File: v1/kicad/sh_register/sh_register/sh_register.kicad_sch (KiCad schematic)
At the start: 4 parts, among them J1 LNCPU_Type_A_connector,_male,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, U1 74LS194, U2 74LS194, U3 74LS245

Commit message: partial
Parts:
- removed J1: LNCPU_Type_A_connector,_male,_active_low_reset, LNCPU:LNCPU_TYPE_A_MALE, symbol lncpu:LNCPU_Type_A_connector,_male,_active_low_reset
- added J1: OP_{out}, Connector_PinSocket_2.54mm:PinSocket_1x08_P2.54mm_Vertical, symbol lncpu:LNCPU_DBUS_Socket
- added U4: LNCPU Type B Connector, lncpu:LNCPU_Type_B_Header, symbol lncpu:LNCPU_Type_B_Connector
- U1, U2: footprint (none) -> Package_DIP:DIP-16_W7.62mm_LongPads
- U3: value 74LS245 -> 74LS244; footprint (none) -> Package_DIP:DIP-20_W7.62mm_LongPads
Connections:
- net ASYNC_{out}0: now also J1.1 (D0)
- net ASYNC_{out}1: now also J1.2 (D1)
- net ASYNC_{out}2: now also J1.3 (D2)
- net ASYNC_{out}3: now also J1.4 (D3)
- net ASYNC_{out}4: now also J1.5 (D4)
- net ASYNC_{out}5: now also J1.6 (D5)
- net ASYNC_{out}6: now also J1.7 (D6)
- net ASYNC_{out}7: now also J1.8 (D7)
- net DBUS0: now also U4.4 (DBUS_{0})
- net DBUS1: now also U4.6 (DBUS_{1})
- net DBUS2: now also U4.8 (DBUS_{2})
- net DBUS3: now also U4.10 (DBUS_{3})
- net DBUS4: now also U4.12 (DBUS_{4})
- net DBUS5: now also U4.14 (DBUS_{5})
- net DBUS6: now also U4.16 (DBUS_{6})
- net DBUS7: now also U4.18 (DBUS_{7})
- net at U1.16 (VCC), U2.16 (VCC), U3.20 (VCC): now also U4.2 (VCC), U4.24 (VCC); no longer U1.1 (Mr), U1.2 (Dsr), U2.1 (Mr)
- net at U1.10 (S1), U2.10 (S1): now also U4.9 (CTRL_{3})
- net at U1.11 (Cp), U2.11 (Cp): now also U4.21 (CLK1)
- net at U1.8 (GND), U2.7 (Dsl), U2.8 (GND)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: now also U1.2 (Dsr), U4.1 (GND), U4.17 (GND), U4.20 (GND), U4.22 (GND)
- net at U1.9 (S0), U2.9 (S0): now also U4.7 (CTRL_{2})
- net at U3.1 (OEa): now also U4.3 (CTRL_{0})
- net at U3.19 (OEb): now also U4.5 (CTRL_{1})
- new net: U1.1 (Mr), U2.1 (Mr), U4.19 (RST)
- no-connect marks 3 -> 4

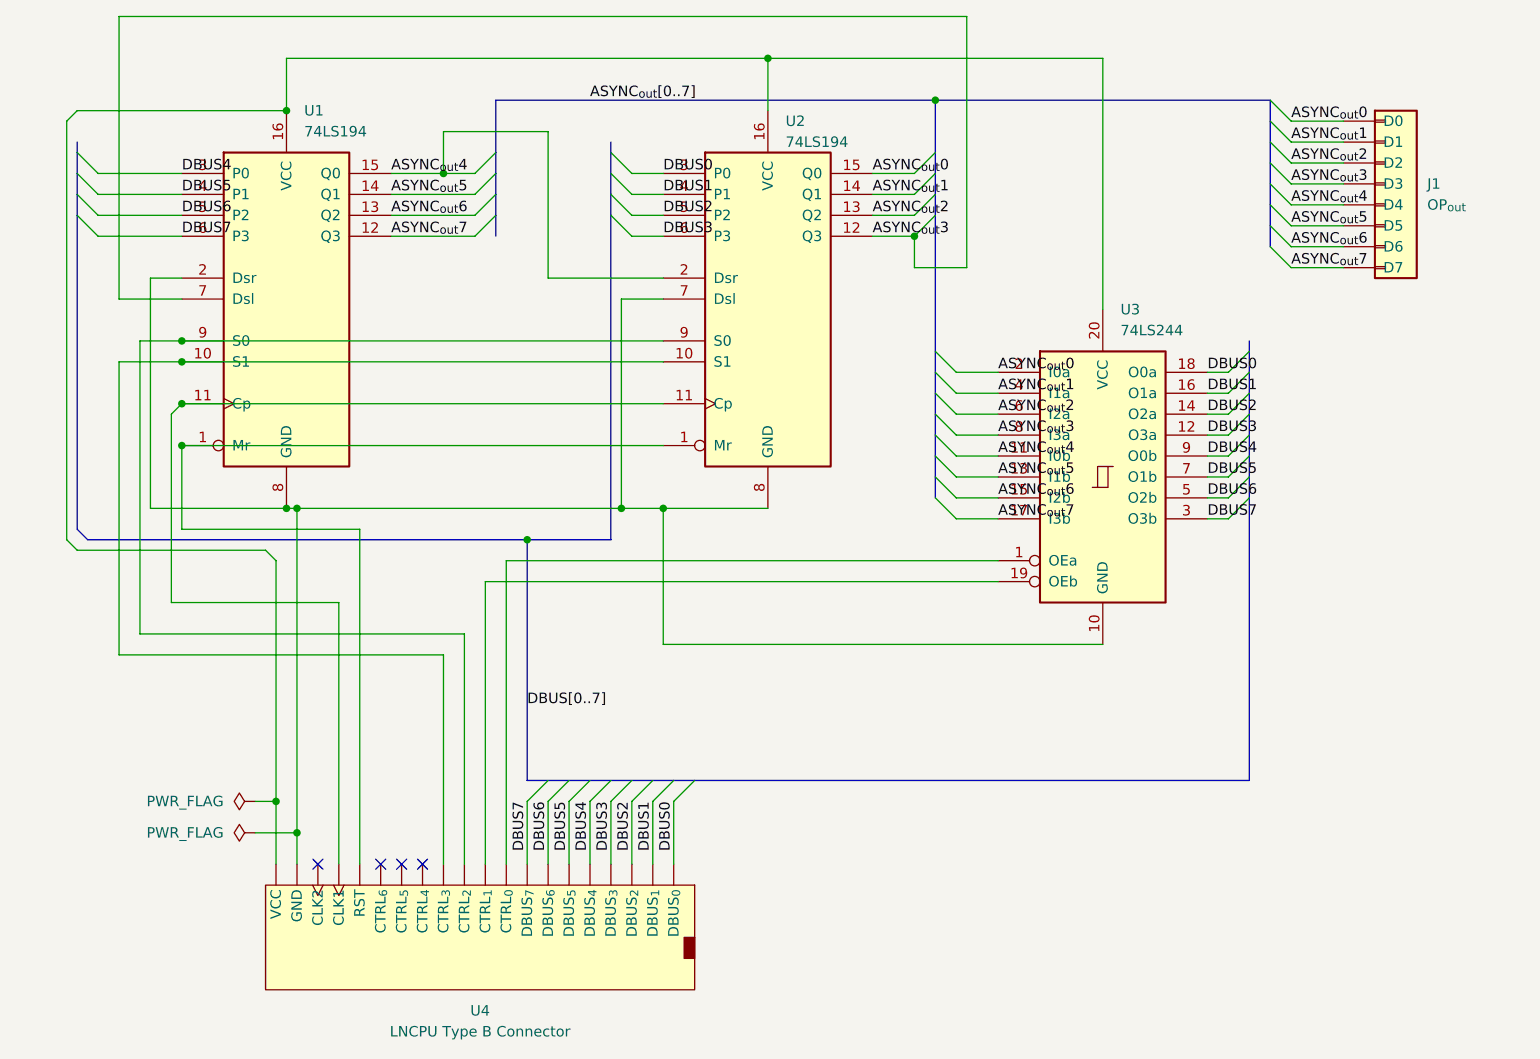
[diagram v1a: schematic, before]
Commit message: check designs for ALU (partial), SP, Shift register, register
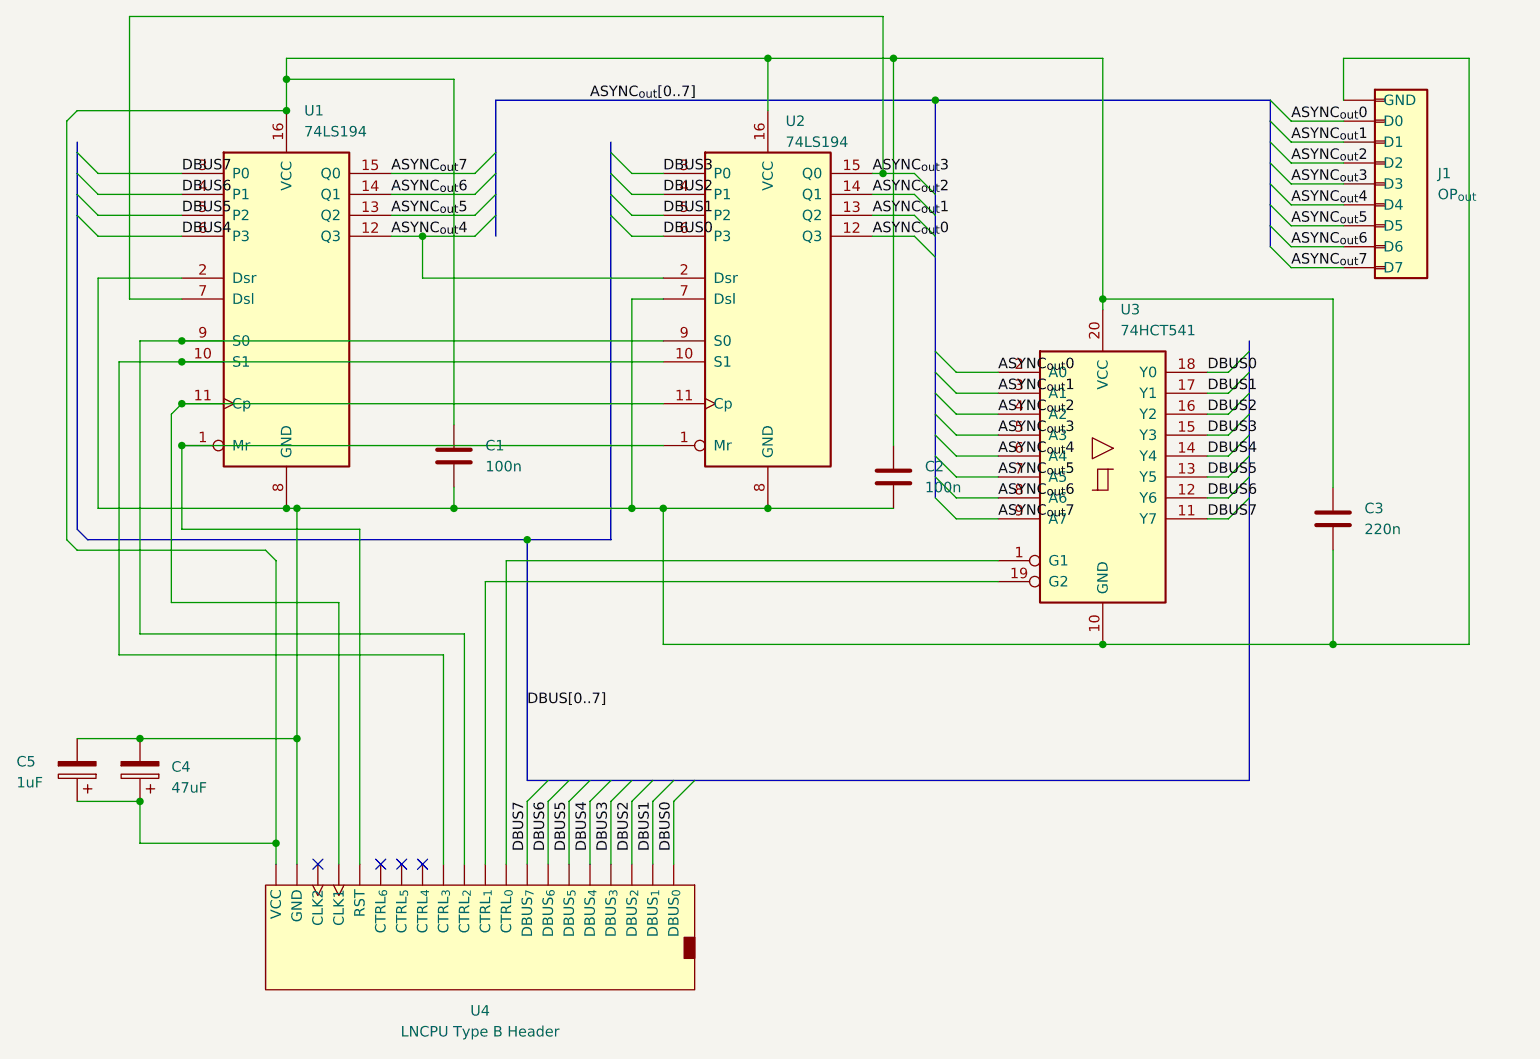
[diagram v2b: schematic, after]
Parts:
- added C1, C2: 100n, Capacitor_THT:C_Disc_D4.3mm_W1.9mm_P5.00mm, symbol Device:C
- added C3: 220n, Capacitor_THT:C_Disc_D4.3mm_W1.9mm_P5.00mm, symbol Device:C
- added C4: 47uF, Capacitor_THT:CP_Radial_D5.0mm_P2.00mm, symbol Device:C_Polarized
- added C5: 1uF, lncpu:CP_Radial_D4.0mm_P2.00mm-Large-Holes, symbol Device:C_Polarized
- J1: footprint Connector_PinSocket_2.54mm:PinSocket_1x08_P2.54mm_Vertical -> Connector_PinSocket_2.54mm:PinSocket_1x10_P2.54mm_Vertical; symbol lncpu:LNCPU_DBUS_Socket -> lncpu:LNCPU_8B_Socket
- U3: value 74LS244 -> 74HCT541; symbol 74xx:74LS244 -> 74xx:74HCT541
- U4: value LNCPU Type B Connector -> LNCPU Type B Header; symbol lncpu:LNCPU_Type_B_Connector -> lncpu:LNCPU_Type_B_Header
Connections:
- net ASYNC_{out}0: now also J1.2 (D0), U2.12 (Q3); no longer J1.1 (D0), U2.15 (Q0)
- net ASYNC_{out}1: now also J1.3 (D1), U2.13 (Q2), U3.3 (A1); no longer J1.2 (D1), U2.14 (Q1), U3.4 (I1a)
- net ASYNC_{out}2: now also J1.4 (D2), U2.14 (Q1), U3.4 (A2); no longer J1.3 (D2), U2.13 (Q2), U3.6 (I2a)
- net ASYNC_{out}3: now also J1.5 (D3), U2.15 (Q0), U3.5 (A3); no longer J1.4 (D3), U2.12 (Q3), U3.8 (I3a)
- net ASYNC_{out}4: now also J1.6 (D4), U1.12 (Q3), U3.6 (A4); no longer J1.5 (D4), U1.15 (Q0), U3.11 (I0b)
- net ASYNC_{out}5: now also J1.7 (D5), U1.13 (Q2), U3.7 (A5); no longer J1.6 (D5), U1.14 (Q1), U3.13 (I1b)
- net ASYNC_{out}6: now also J1.8 (D6), U1.14 (Q1), U3.8 (A6); no longer J1.7 (D6), U1.13 (Q2), U3.15 (I2b)
- net ASYNC_{out}7: now also J1.9 (D7), U1.15 (Q0), U3.9 (A7); no longer J1.8 (D7), U1.12 (Q3), U3.17 (I3b)
- net DBUS0: now also U2.6 (P3); no longer U2.3 (P0)
- net DBUS1: now also U2.5 (P2), U3.17 (Y1); no longer U2.4 (P1), U3.16 (O1a)
- net DBUS2: now also U2.4 (P1), U3.16 (Y2); no longer U2.5 (P2), U3.14 (O2a)
- net DBUS3: now also U2.3 (P0), U3.15 (Y3); no longer U2.6 (P3), U3.12 (O3a)
- net DBUS4: now also U1.6 (P3), U3.14 (Y4); no longer U1.3 (P0), U3.9 (O0b)
- net DBUS5: now also U1.5 (P2), U3.13 (Y5); no longer U1.4 (P1), U3.7 (O1b)
- net DBUS6: now also U1.4 (P1), U3.12 (Y6); no longer U1.5 (P2), U3.5 (O2b)
- net DBUS7: now also U1.3 (P0), U3.11 (Y7); no longer U1.6 (P3), U3.3 (O3b)
- net at U1.16 (VCC), U2.16 (VCC), U3.20 (VCC)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: now also C1.1, C2.1, C3.1, C4.1, C5.1
- net at U1.2 (Dsr), U1.8 (GND), U2.7 (Dsl)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: now also J1.1 (GND), J1.10 (GND), C1.2, C2.2, C3.2, C4.2, C5.2

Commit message: readapt designs for BR, SP, SR, ALU
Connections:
- net DBUS0: now also U4.3 (DBUS_{0}); no longer U4.4 (DBUS_{0})
- net DBUS1: now also U4.5 (DBUS_{1}); no longer U4.6 (DBUS_{1})
- net DBUS2: now also U4.7 (DBUS_{2}); no longer U4.8 (DBUS_{2})
- net DBUS3: now also U4.9 (DBUS_{3}); no longer U4.10 (DBUS_{3})
- net DBUS4: now also U4.11 (DBUS_{4}); no longer U4.12 (DBUS_{4})
- net DBUS5: now also U4.13 (DBUS_{5}); no longer U4.14 (DBUS_{5})
- net DBUS6: now also U4.15 (DBUS_{6}); no longer U4.16 (DBUS_{6})
- net DBUS7: now also U4.17 (DBUS_{7}); no longer U4.18 (DBUS_{7})
- net at C1.1, C2.1, C3.1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: now also J1.10 (VCC)
- net at C1.2, C2.2, C3.2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: now also U4.18 (GND), U4.23 (GND); no longer J1.10 (GND), U4.17 (GND), U4.20 (GND)
- net at U1.10 (S1), U2.10 (S1): now also U4.10 (CTRL_{3}); no longer U4.9 (CTRL_{3})
- net at U1.9 (S0), U2.9 (S0): now also U4.8 (CTRL_{2}); no longer U4.7 (CTRL_{2})
- net at U3.1 (G1): now also U4.4 (CTRL_{0}); no longer U4.3 (CTRL_{0})
- net at U3.19 (G2): now also U4.6 (CTRL_{1}); no longer U4.5 (CTRL_{1})
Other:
- moved on the sheet: U4
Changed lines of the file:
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@@
+	)
+	(junction
+		(at 228.6 60.96)
+		(diameter 0)
+		(color 0 0 0 0)
 	)
 	(junction
@@
 		)
 	)
+	(wire
+		(pts
+			(xy 228.6 59.69) (xy 228.6 60.96)
+		)
+		(stroke
+			(width 0)
+			(type default)
+		)
+	)
 	(bus
 		(pts
@@
 		)
 		(stroke
+			(width 0)
+			(type default)
+		)
+	)
+	(wire
+		(pts
+			(xy 229.87 59.69) (xy 228.6 59.69)
+		)
+		(stroke
